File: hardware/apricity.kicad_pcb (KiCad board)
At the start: 2 copper layers, 71.2 x 71.2 mm, 55 parts, among them J1 Conn_01x03_Male, J2 USB_C_Receptacle_USB2.0, SW1 Reset, SW2 Prog, U1 ESP-WROOM-02D, U2 AP2210N-3.3TRG1

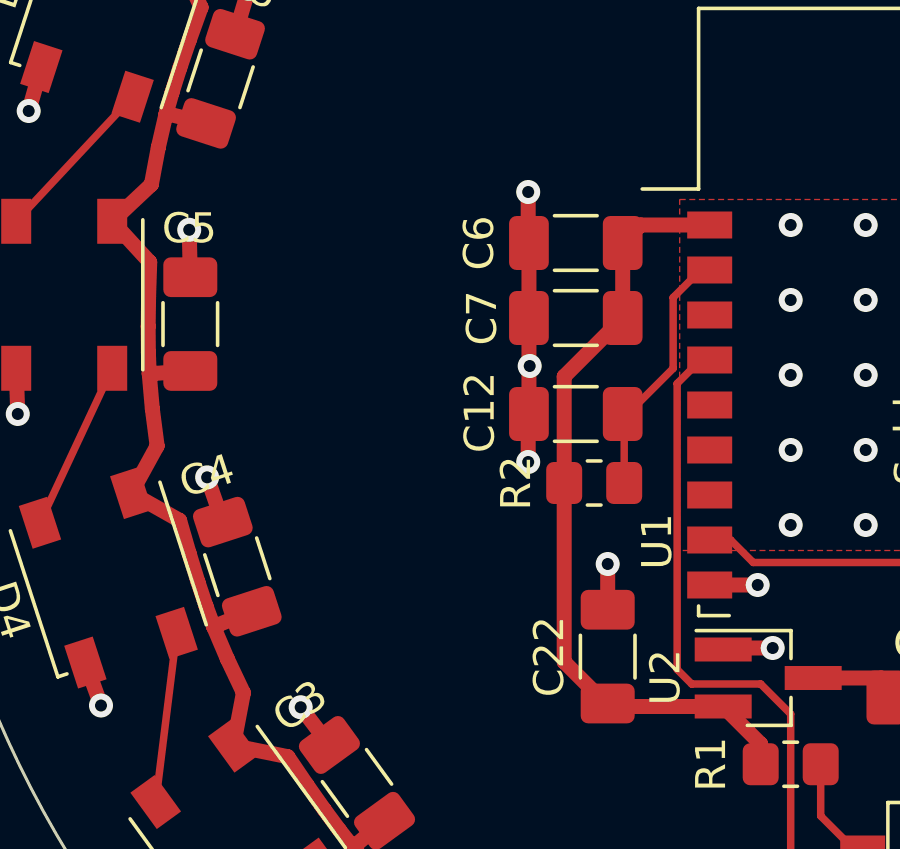
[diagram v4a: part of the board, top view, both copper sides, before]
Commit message: add power test points
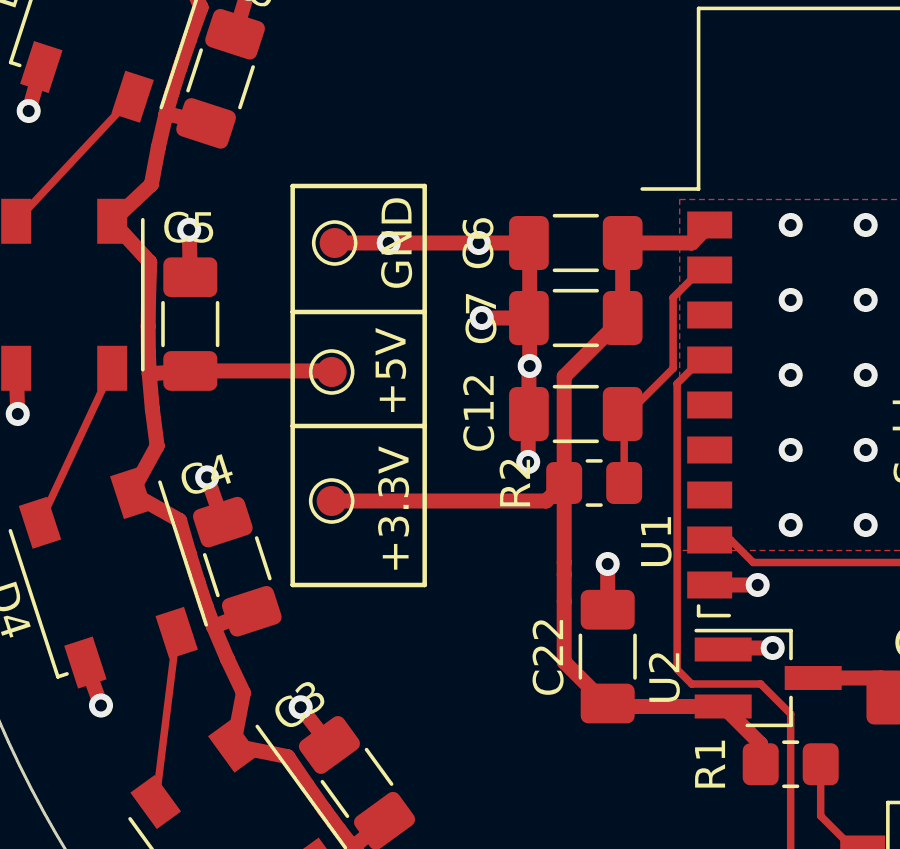
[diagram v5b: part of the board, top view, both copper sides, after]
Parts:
- added TP1: TestPoint, TestPoint:TestPoint_Pad_D1.0mm, F.Cu at (126.4, 100.8)
- added TP2: TestPoint, TestPoint:TestPoint_Pad_D1.0mm, F.Cu at (126.5, 92.2)
- added TP3: TestPoint, TestPoint:TestPoint_Pad_D1.0mm, F.Cu at (126.4, 96.5)
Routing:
- net +3.3V: track 26.3 -> 34.3 mm
- net GND: track 83.7 -> 90.0 mm, vias 74 -> 76
- net +5V: track 227.0 -> 231.7 mm
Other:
- board text added: "+3.3V"
- board text added: "+5V"

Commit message: tweak test point positions
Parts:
- moved TP2 2.40 mm to (126.5, 89.8)
- moved TP3 2.40 mm to (126.4, 94.1)
- moved TP1 2.40 mm to (126.4, 98.4)
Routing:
- net GND: track 90.0 -> 92.8 mm, vias 76 -> 77
- net +5V: track 231.7 -> 232.7 mm

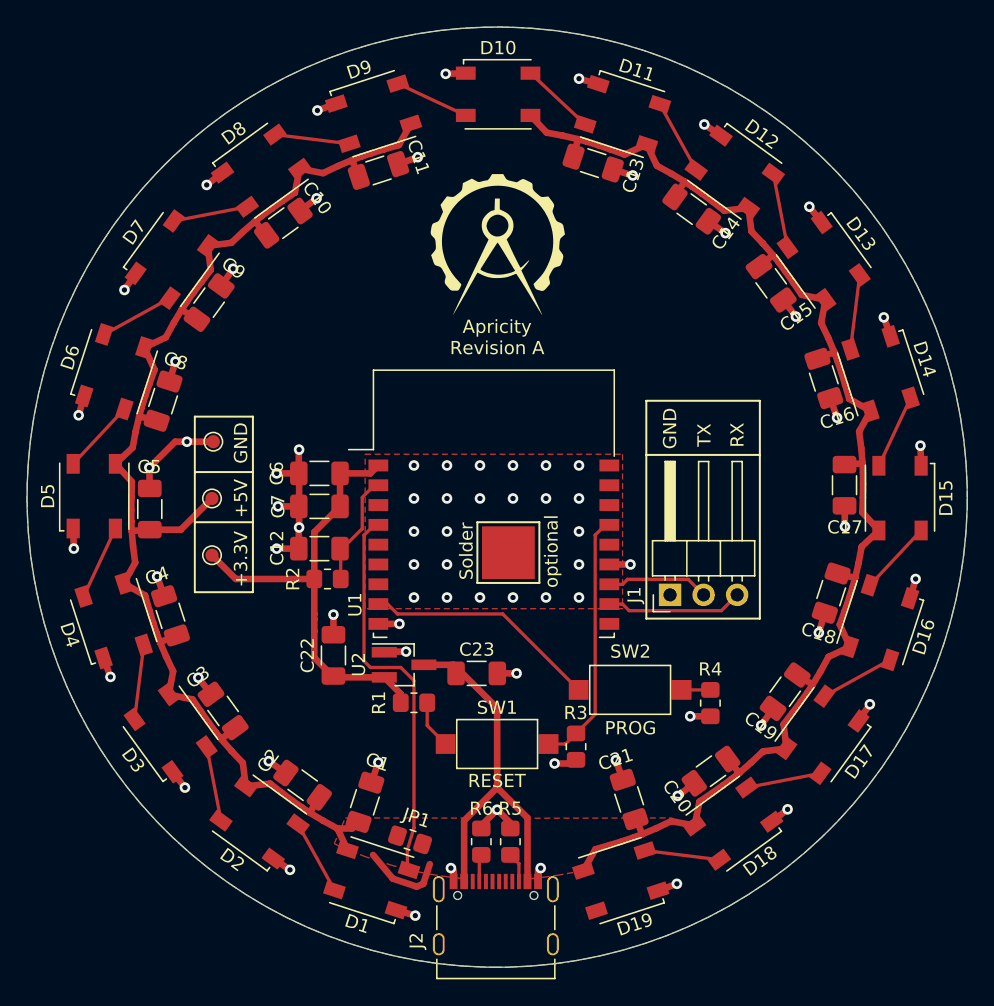
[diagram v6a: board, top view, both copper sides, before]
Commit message: make room for usb c controller
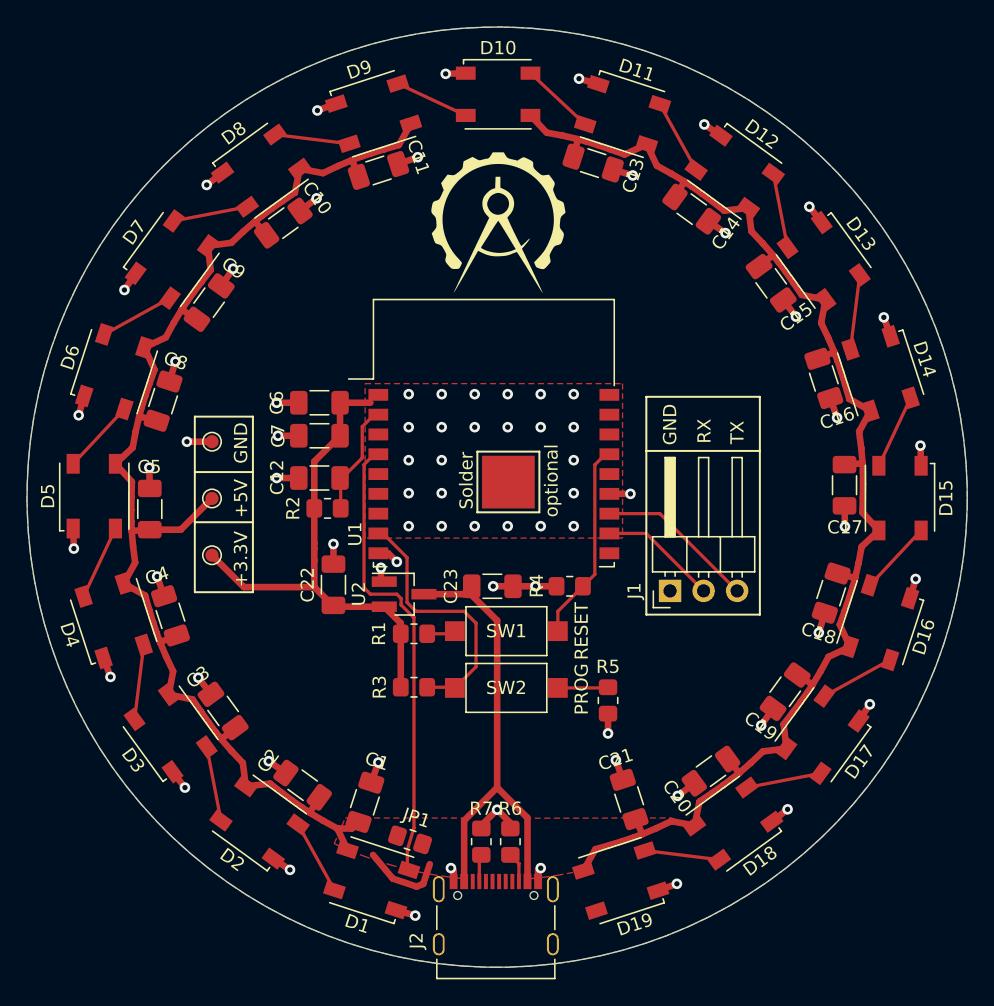
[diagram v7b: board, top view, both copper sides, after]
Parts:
- added R3: 100, Resistor_SMD:R_0805_2012Metric_Pad1.20x1.40mm_HandSolder, F.Cu at (141.7, 108.4)
- moved R4 12.2 mm to (153.5, 100.8), turned to 180 degrees
- moved SW2 9.38 mm to (148.7, 108.5)
- moved SW1 8.58 mm to (148.7, 104.2)
- moved R5 7.75 mm to (156.4, 109.4)
- moved C23 6.71 mm to (147.6, 100.8)
- moved C12 5.35 mm to (134.5, 92.5)
- moved C6 5.35 mm to (134.5, 86.8)
- moved C7 5.35 mm to (134.5, 89.3)
- moved R2 5.35 mm to (135.2, 94.8)
- moved U2 5.35 mm to (140.9, 101.3)
- moved C22 5.35 mm to (135.6, 100.6)
- moved U1 5.35 mm to (147.8, 92.2)
- moved R1 5.23 mm to (141.7, 104.3)
- moved J1 0.30 mm to (161.1, 101.1)
- moved TP2 0.10 mm to (126.4, 89.8)
- renumbered R3 to R4, R4 to R5, R5 to R6, R6 to R7
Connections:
- J1 pad 2: Net-(J1-Pad2) -> Net-(U1-Pad11)
- J1 pad 3: Net-(J1-Pad3) -> Net-(U1-Pad12)
- U1 pad 11: Net-(J1-Pad3) -> Net-(U1-Pad11)
- U1 pad 12: Net-(J1-Pad2) -> Net-(U1-Pad12)
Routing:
- net Net-(U1-Pad12): track 0.00 -> 12.1 mm
- net Net-(J1-Pad3): track 10.4 -> 0.00 mm
- net GND: track 92.8 -> 82.5 mm, vias 77 -> 75
- net Net-(U1-Pad11): track 0.00 -> 8.94 mm
- net Net-(J1-Pad2): track 7.78 -> 0.00 mm
- net +5V: track 232.7 -> 239.6 mm
- net /LED: track 29.8 -> 34.7 mm
- net Net-(R4-Pad1): track 19.4 -> 15.2 mm
- net +3.3V: track 34.8 -> 38.4 mm
- net Net-(SW2-Pad1): track 17.9 -> 19.9 mm
- net Net-(R5-Pad1): track 2.18 -> 3.82 mm
- net Net-(R1-Pad2): track 3.70 -> 2.18 mm
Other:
- board text removed: "Apricity Revision A"

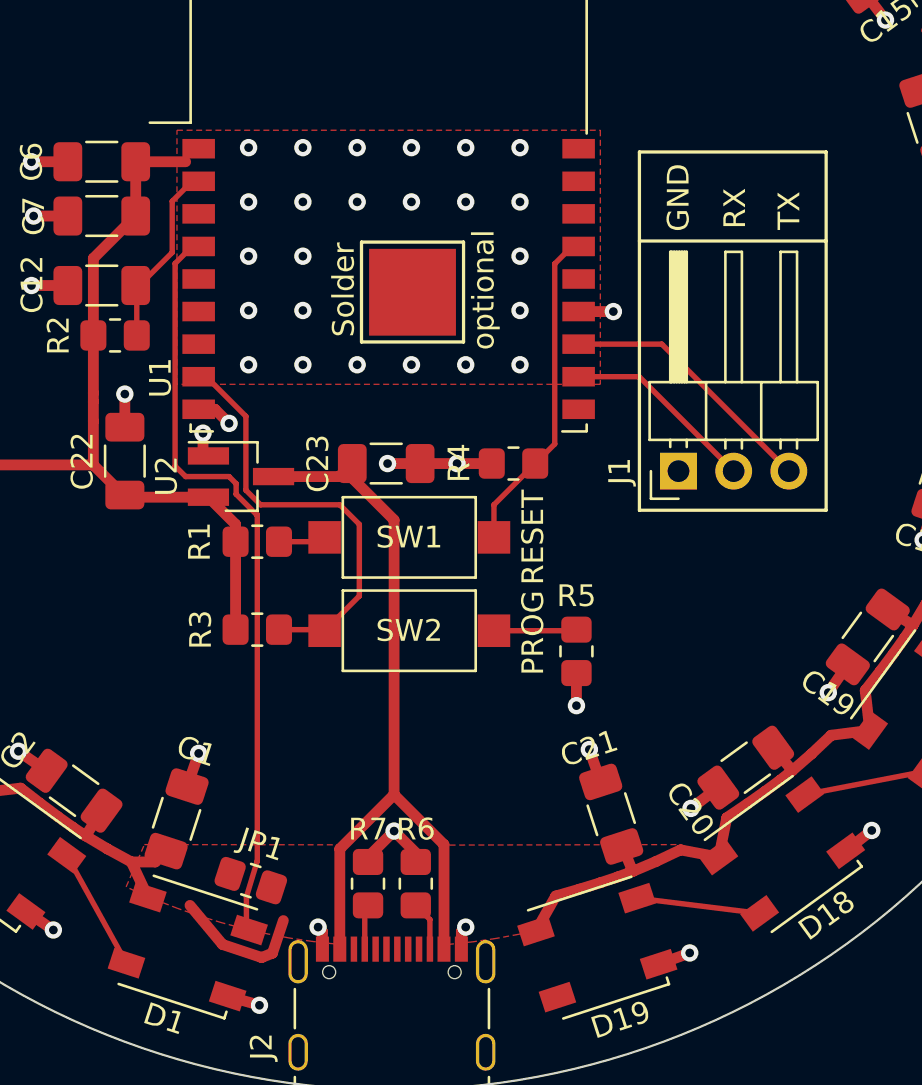
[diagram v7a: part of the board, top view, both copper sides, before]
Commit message: add analogue switch for checking current supply
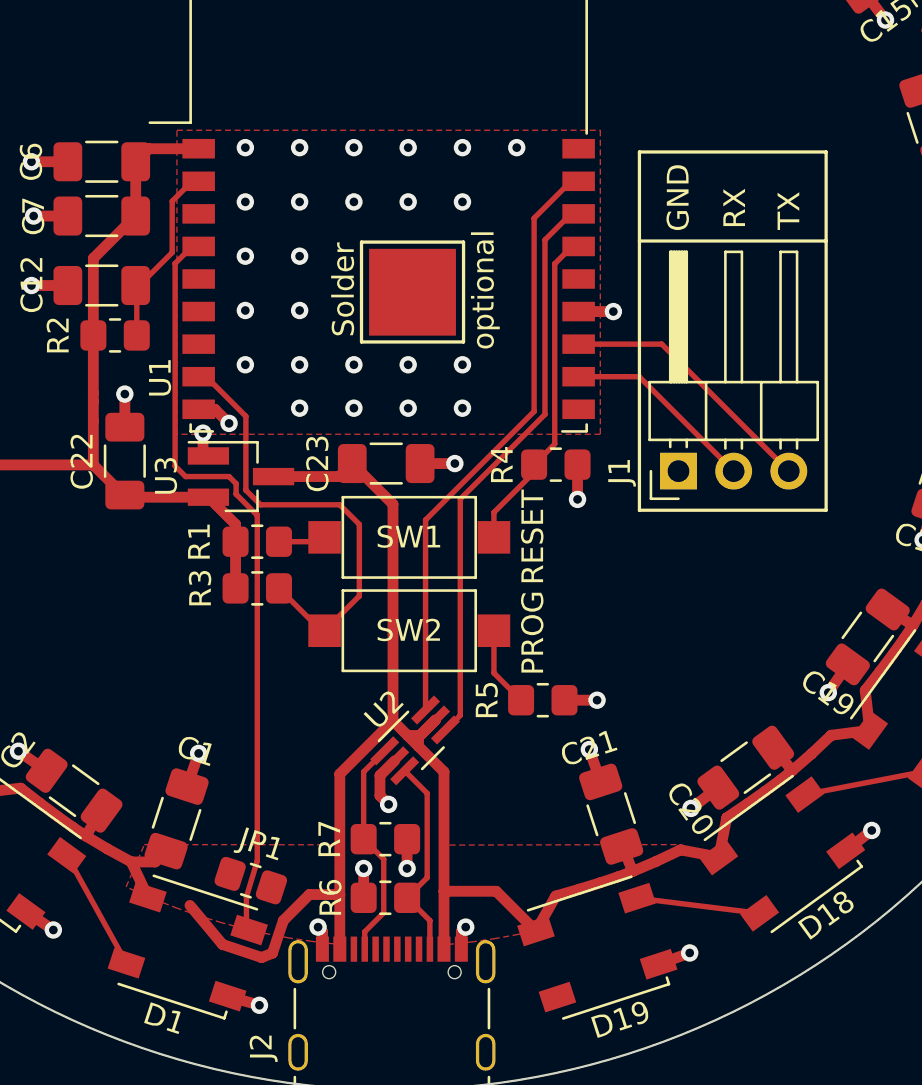
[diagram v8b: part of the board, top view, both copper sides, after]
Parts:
- added U2: NC7SB3157, Package_TO_SOT_SMD:SOT-363_SC-70-6_Handsoldering, F.Cu at (149.0, 113.5)
- moved R5 2.73 mm to (154.8, 111.7), turned to 0 degrees
- moved R7 2.20 mm to (147.6, 118.0), turned to 0 degrees
- moved R4 1.95 mm to (155.4, 100.8), turned to 0 degrees
- moved R3 1.90 mm to (141.7, 106.5)
- moved R6 1.54 mm to (147.6, 120.8), turned to 180 degrees
- renumbered U2 to U3
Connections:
- net Net-(J2-PadA5) renamed /CC1
- net Net-(J2-PadB5) renamed /CC2
- U1 pad 16: unconnected-(U1-Pad16) -> /TOUT
- U1 pad 17: unconnected-(U1-Pad17) -> /IO16
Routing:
- net /IO16: track 0.00 -> 27.5 mm
- net /TOUT: track 0.00 -> 26.5 mm
- net +5V: track 239.6 -> 254.2 mm
- net /CC1: track 2.08 -> 10.3 mm
- net /CC2: track 2.28 -> 9.46 mm
- net +3.3V: track 38.4 -> 37.3 mm
- net Net-(R3-Pad2): track 19.9 -> 20.7 mm
- net GND: track 82.5 -> 82.3 mm, vias 75 -> 77
